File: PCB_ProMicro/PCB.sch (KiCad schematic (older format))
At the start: 98 parts, among them SW1 SW_Push, SW10 SW_Push, SW11 SW_Push, SW12 SW_Push, SW13 SW_Push, SW14 SW_Push, SW15 SW_Push, SW16 SW_Push, SW17 SW_Push, SW18 SW_Push, SW19 SW_Push, SW2 SW_Push, SW20 SW_Push, SW21 SW_Push, SW22 SW_Push, SW23 SW_Push, SW24 SW_Push, SW25 SW_Push, SW26 SW_Push, SW27 SW_Push, SW28 SW_Push, SW29 SW_Push, SW3 SW_Push, SW30 SW_Push, SW31 SW_Push, SW32 SW_Push, SW33 SW_Push, SW34 SW_Push, SW35 SW_Push, SW36 SW_Push, SW37 SW_Push, SW38 SW_Push, SW39 SW_Push, SW4 SW_Push, SW40 SW_Push, SW41 SW_Push, SW42 SW_Push, SW43 SW_Push, SW44 SW_Push, SW45 SW_Push, SW46 SW_Push, SW47 SW_Push, SW48 SW_Push, SW49 SW_Push, SW5 SW_Push, SW6 SW_Push, SW7 SW_Push, SW8 SW_Push, SW9 SW_Push

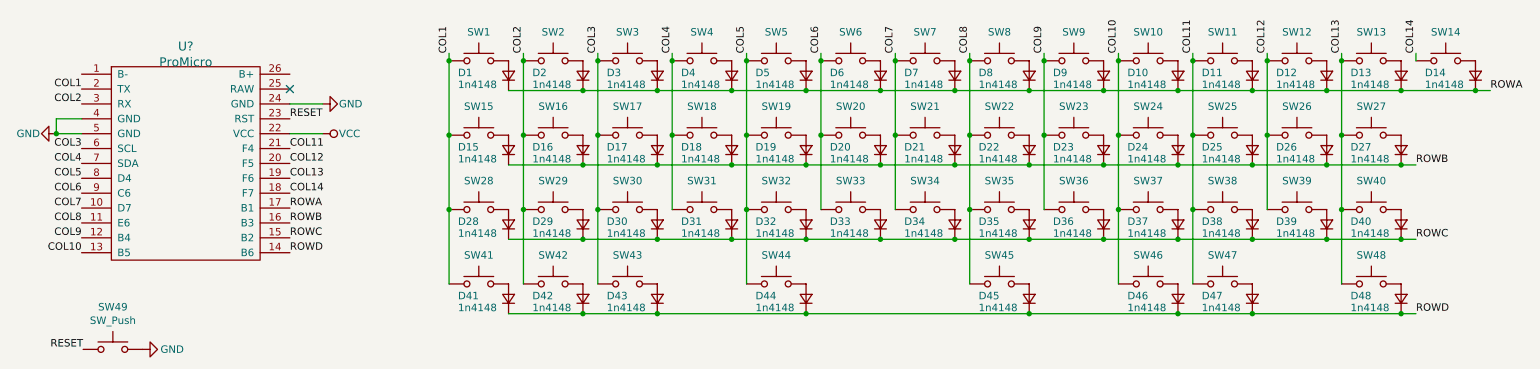
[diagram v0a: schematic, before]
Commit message: Edit pro micro symbol
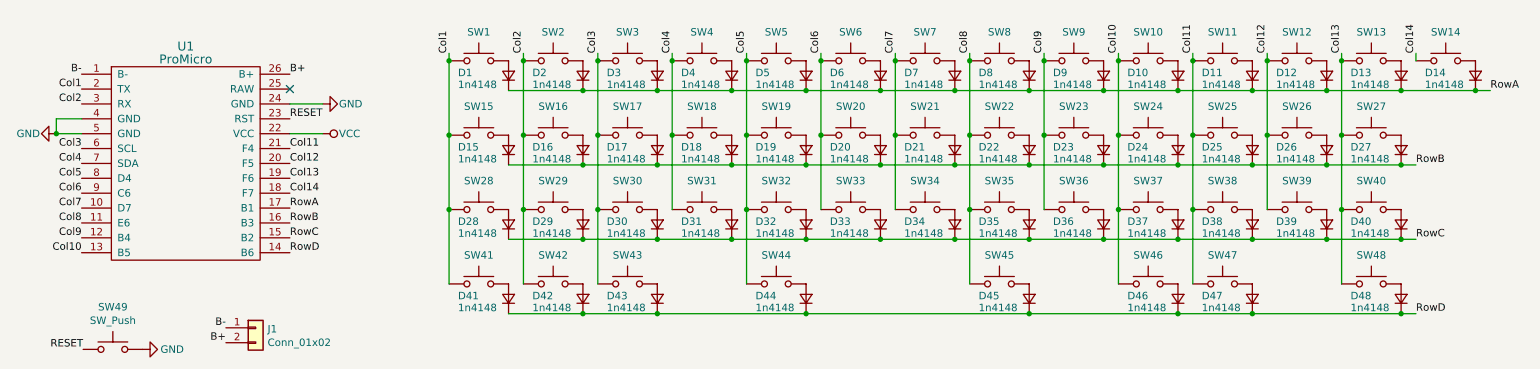
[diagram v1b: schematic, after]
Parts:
- added J1: Conn_01x02, symbol Connector_Generic:Conn_01x02
- gave numbers to parts that had none: 1
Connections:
- net B-: now reaches U1.1 (B-)
- net B-: now also J1.1 (Pin_1)
- net B+: now reaches U1.26 (B+)
- net B+: now also J1.2 (Pin_2)
- net COL1 renamed Col1
- net COL10 renamed Col10
- net COL11 renamed Col11
- net COL12 renamed Col12
- net COL13 renamed Col13
- net COL14 renamed Col14
- net COL2 renamed Col2
- net COL3 renamed Col3
- net COL4 renamed Col4
- net COL5 renamed Col5
- net COL6 renamed Col6
- net COL7 renamed Col7
- net COL8 renamed Col8
- net COL9 renamed Col9
- net ROWA renamed RowA
- net ROWB renamed RowB
- net ROWC renamed RowC
- net ROWD renamed RowD
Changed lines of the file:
@@
 	9800 2380 9300 2380
 Text Label 3900 1130 1    50   ~ 0
-COL1
+Col1
 Text Label 4400 1130 1    50   ~ 0
-COL2
+Col2
 Text Label 4900 1130 1    50   ~ 0
-COL3
+Col3
 Text Label 5400 1130 1    50   ~ 0
-COL4
+Col4
 Text Label 5900 1130 1    50   ~ 0
-COL5
+Col5
 Text Label 6400 1130 1    50   ~ 0
-COL6
+Col6
 Text Label 6900 1130 1    50   ~ 0
-COL7
+Col7
 Text Label 7400 1130 1    50   ~ 0
-COL8
+Col8
 Text Label 7900 1130 1    50   ~ 0
-COL9
+Col9
 Text Label 8400 1130 1    50   ~ 0
-COL10
+Col10
 Text Label 8900 1130 1    50   ~ 0
-COL11
+Col11
 Text Label 9400 1130 1    50   ~ 0
-COL12
+Col12
 Text Label 9900 1130 1    50   ~ 0
-COL13
+Col13
 Text Label 10400 1130 1    50   ~ 0
-COL14
+Col14
 Text Label 10900 1380 0    50   ~ 0
-ROWA
+RowA
 Text Label 10400 1880 0    50   ~ 0
-ROWB
+RowB
 Text Label 10400 2380 0    50   ~ 0
-ROWC
+RowC
 Wire Wire Line
 	10400 2380 10300 2380
@@
 	9300 2880 10300 2880
 Text Label 10400 2880 0    50   ~ 0
-ROWD
+RowD
 Wire Wire Line
 	10400 2880 10300 2880
@@
 $EndComp
 $Comp
-L promicro:ProMicro U?
+L promicro:ProMicro U1
 U 1 1 5ED7E469
 P 2130 2120
-F 0 "U?" H 2130 3157 60  0000 C CNN
-F 1 "ProMicro" H 2130 3051 60  0000 C CNN
+F 0 "U1" H 2130 3157 60  0000 C CNN
+F 1 "ProMicro" H 2130 3070 60  0000 C CNN
 F 2 "" H 2230 1070 60  0000 C CNN
 F 3 "" H 2230 1070 60  0000 C CNN
@@
 $EndComp
 $Comp
-L power:GND #PWR?
+L power:GND #PWR0101
 U 1 1 5ED825B3
 P 3050 1470
-F 0 "#PWR?" H 3050 1220 50  0001 C CNN
+F 0 "#PWR0101" H 3050 1220 50  0001 C CNN
 F 1 "GND" V 3050 1360 50  0000 R CNN
 F 2 "" H 3050 1470 50  0001 C CNN
@@
 $EndComp
 $Comp
-L power:GND #PWR?
+L power:GND #PWR0102
 U 1 1 5ED85438
 P 1260 1670
-F 0 "#PWR?" H 1260 1420 50  0001 C CNN
+F 0 "#PWR0102" H 1260 1420 50  0001 C CNN
 F 1 "GND" V 1260 1560 50  0000 R CNN
 F 2 "" H 1260 1670 50  0001 C CNN
@@
 $EndComp
 $Comp
-L power:VCC #PWR?
+L power:VCC #PWR0103
 U 1 1 5ED8AD67
 P 3050 1670
-F 0 "#PWR?" H 3050 1520 50  0001 C CNN
+F 0 "#PWR0103" H 3050 1520 50  0001 C CNN
 F 1 "VCC" V 3050 1780 50  0000 L CNN
 F 2 "" H 3050 1670 50  0001 C CNN
@@
 NoConn ~ 2830 1370
 Text Label 1430 1370 2    50   ~ 0
-COL1
+Col1
 Text Label 1430 1470 2    50   ~ 0
-COL2
+Col2
 Text Label 1430 1770 2    50   ~ 0
-COL3
+Col3
 Text Label 1430 1870 2    50   ~ 0
-COL4
+Col4
 Text Label 1430 2070 2    50   ~ 0
-COL6
+Col6
 Text Label 1430 1970 2    50   ~ 0
-COL5
+Col5
 Text Label 1430 2170 2    50   ~ 0
-COL7
+Col7
 Text Label 1430 2270 2    50   ~ 0
-COL8
+Col8
 Text Label 1430 2370 2    50   ~ 0
-COL9
+Col9
 Text Label 1430 2470 2    50   ~ 0
-COL10
+Col10
 Wire Wire Line
 	1260 1670 1430 1670
@@
 Connection ~ 1260 1670
 Text Label 2830 1770 0    50   ~ 0
-COL11
+Col11
 Text Label 2830 1870 0    50   ~ 0
-COL12
+Col12
 Text Label 2830 1970 0    50   ~ 0
-COL13
+Col13
 Text Label 2830 2070 0    50   ~ 0
-COL14
+Col14
 Text Label 2830 2170 0    50   ~ 0
-ROWA
+RowA
 Text Label 2830 2270 0    50   ~ 0
-ROWB
+RowB
 Text Label 2830 2370 0    50   ~ 0
-ROWC
+RowC
 Text Label 2830 2470 0    50   ~ 0
-ROWD
+RowD
 Text Label 2830 1570 0    50   ~ 0
 RESET
@@
 Text Label 1440 3120 2    50   ~ 0
 RESET
+$Comp
+L Connector_Generic:Conn_01x02 J1
+U 1 1 5ED706FC
+P 2600 2975
+F 0 "J1" H 2680 2967 50  0000 L CNN
+F 1 "Conn_01x02" H 2680 2876 50  0000 L CNN
+F 2 "" H 2600 2975 50  0001 C CNN
+F 3 "~" H 2600 2975 50  0001 C CNN
+	1    2600 2975
+	1    0    0    -1
+$EndComp
+Text Label 2400 2975 2    50   ~ 0
+B-
+Text Label 2400 3075 2    50   ~ 0
+B+
+Text Label 1430 1270 2    50   ~ 0
+B-
+Text Label 2830 1270 0    50   ~ 0
+B+
 $EndSCHEMATC

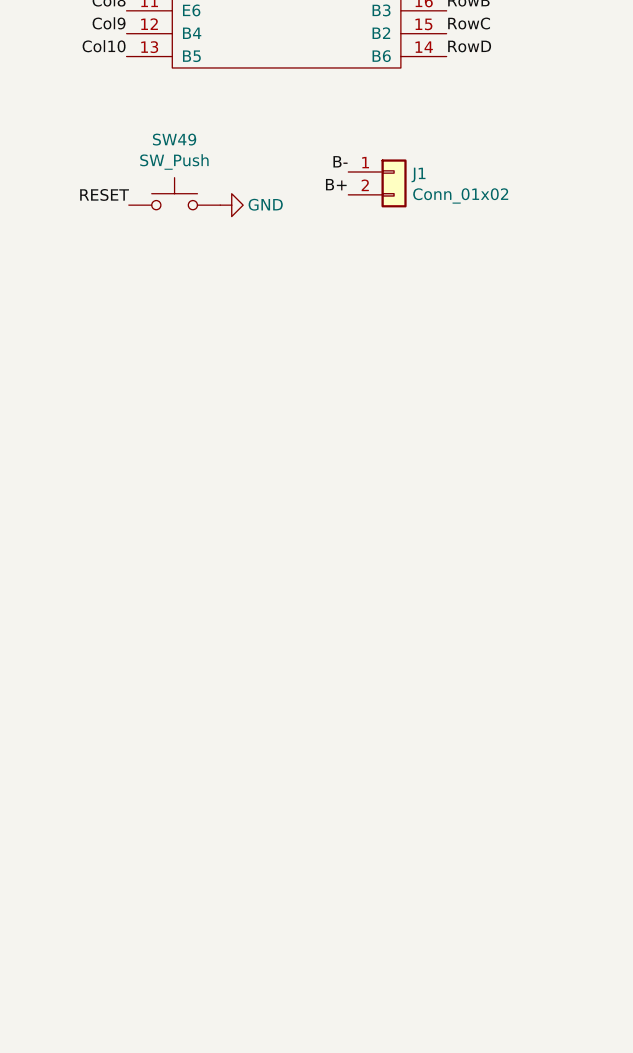
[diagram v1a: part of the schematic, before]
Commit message: Add USB-C into schematic
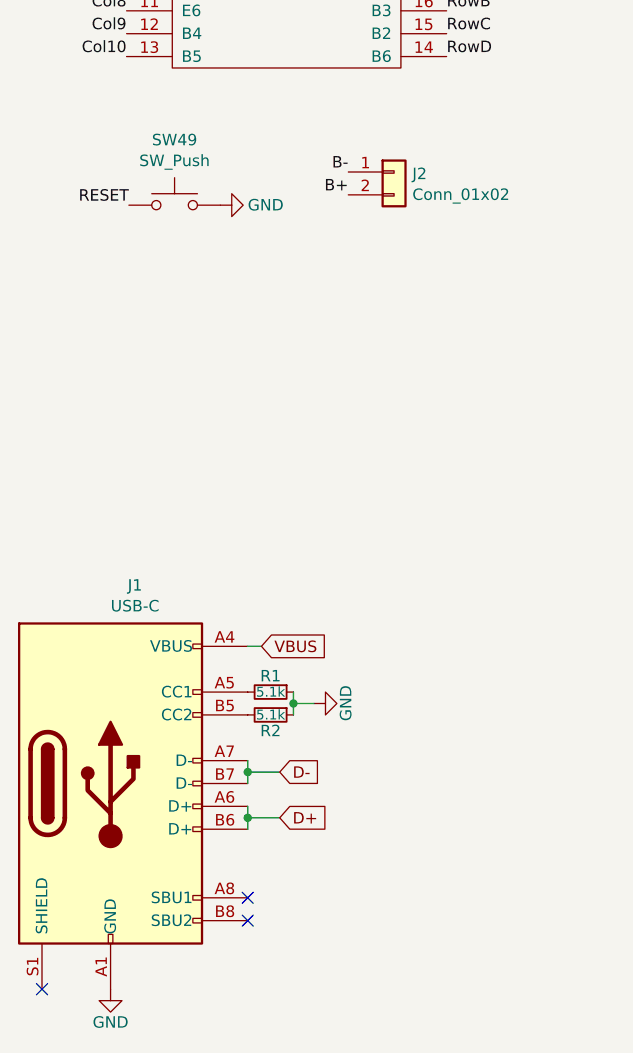
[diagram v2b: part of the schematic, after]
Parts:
- added J1: USB-C, symbol Connector:USB_C_Receptacle_USB2.0
- added R1, R2: 5.1k, symbol Device:R_Small
- renumbered J1 to J2
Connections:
- net GND: now also J1.A1 (GND), J1.A12 (GND), J1.B1 (GND), J1.B12 (GND), R1.1, R2.1
- new net: J1.A5 (CC1), R1.2
- new net: J1.B5 (CC2), R2.2
- new net D+: J1.A6 (D+), J1.B6 (D+)
- new net D-: J1.A7 (D-), J1.B7 (D-)
- new net VBUS: J1.A4 (VBUS), J1.A9 (VBUS), J1.B4 (VBUS), J1.B9 (VBUS)
- no-connect marks 1 -> 4
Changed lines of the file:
@@
 RESET
 $Comp
-L Connector_Generic:Conn_01x02 J1
+L Connector_Generic:Conn_01x02 J2
 U 1 1 5ED706FC
 P 2600 2975
-F 0 "J1" H 2680 2967 50  0000 L CNN
+F 0 "J2" H 2680 2967 50  0000 L CNN
 F 1 "Conn_01x02" H 2680 2876 50  0000 L CNN
 F 2 "" H 2600 2975 50  0001 C CNN
@@
 Text Label 2830 1270 0    50   ~ 0
 B+
+$Comp
+L Connector:USB_C_Receptacle_USB2.0 J1
+U 1 1 5EDB247E
+P 1360 5650
+F 0 "J1" H 1467 6517 50  0000 C CNN
+F 1 "USB-C" H 1467 6426 50  0000 C CNN
+F 2 "" H 1510 5650 50  0001 C CNN
+F 3 "https://www.usb.org/sites/default/files/documents/usb_type-c.zip" H 1510 5650 50  0001 C CNN
+	1    1360 5650
+	1    0    0    -1
+$EndComp
+Text GLabel 2100 5600 2    50   Input ~ 0
+D-
+Wire Wire Line
+	1960 5550 1960 5600
+Wire Wire Line
+	2100 5600 1960 5600
+Connection ~ 1960 5600
+Wire Wire Line
+	1960 5600 1960 5650
+Text GLabel 2100 5800 2    50   Input ~ 0
+D+
+Wire Wire Line
+	1960 5750 1960 5800
+Wire Wire Line
+	2100 5800 1960 5800
+Connection ~ 1960 5800
+Wire Wire Line
+	1960 5800 1960 5850
+$Comp
+L power:GND #PWR?
+U 1 1 5EDC59F6
+P 1360 6550
+F 0 "#PWR?" H 1360 6300 50  0001 C CNN
+F 1 "GND" H 1360 6405 50  0000 C CNN
+F 2 "" H 1360 6550 50  0001 C CNN
+F 3 "" H 1360 6550 50  0001 C CNN
+	1    1360 6550
+	1    0    0    -1
+$EndComp
+$Comp
+L Device:R_Small R1
+U 1 1 5EDC6E57
+P 2060 5250
+F 0 "R1" V 1990 5250 50  0000 C CNN
+F 1 "5.1k" V 2060 5250 43  0000 C CNN
+F 2 "" H 2060 5250 50  0001 C CNN
+F 3 "~" H 2060 5250 50  0001 C CNN
+	1    2060 5250
+	0    1    1    0
+$EndComp
+$Comp
+L Device:R_Small R2
+U 1 1 5EDC82FE
+P 2060 5350
+F 0 "R2" V 2130 5350 50  0000 C CNN
+F 1 "5.1k" V 2060 5350 43  0000 C CNN
+F 2 "" H 2060 5350 50  0001 C CNN
+F 3 "~" H 2060 5350 50  0001 C CNN
+	1    2060 5350
+	0    1    1    0
+$EndComp
+$Comp
+L power:GND #PWR?
+U 1 1 5EDCBE4E
+P 2250 5300
+F 0 "#PWR?" H 2250 5050 50  0001 C CNN
+F 1 "GND" H 2330 5160 50  0000 R CNN
+F 2 "" H 2250 5300 50  0001 C CNN
+F 3 "" H 2250 5300 50  0001 C CNN
+	1    2250 5300
+	0    -1   -1   0
+$EndComp
+Wire Wire Line
+	2160 5250 2160 5300
+Wire Wire Line
+	2250 5300 2160 5300
+Connection ~ 2160 5300
+Wire Wire Line
+	2160 5300 2160 5350
+Text GLabel 2020 5050 2    50   Input ~ 0
+VBUS
+Wire Wire Line
+	2020 5050 1960 5050
+NoConn ~ 1060 6550
+NoConn ~ 1960 6150
+NoConn ~ 1960 6250
 $EndSCHEMATC

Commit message: Add ESD protection diode
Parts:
- added U?: USBLC6-2SC6, Package_TO_SOT_SMD:SOT-23-6, symbol Power_Protection:USBLC6-2SC6
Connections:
- net D+: now also U?.1 (IO1); no longer J1.A6 (D+), J1.B6 (D+)
- net D-: now also U?.3 (IO2); no longer J1.A7 (D-), J1.B7 (D-)
- net GND: now also U?.2 (GND)
- net VBUS: now also U?.5 (VBUS)
- new net USB_D+: J1.A6 (D+), J1.B6 (D+), U?.6 (IO1)
- new net USB_D-: J1.A7 (D-), J1.B7 (D-), U?.4 (IO2)
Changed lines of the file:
@@
 $EndComp
 Text GLabel 2100 5600 2    50   Input ~ 0
-D-
+USB_D-
 Wire Wire Line
 	1960 5550 1960 5600
@@
 	1960 5600 1960 5650
 Text GLabel 2100 5800 2    50   Input ~ 0
-D+
+USB_D+
 Wire Wire Line
 	1960 5750 1960 5800
@@
 NoConn ~ 1960 6150
 NoConn ~ 1960 6250
+$Comp
+L Power_Protection:USBLC6-2SC6 U?
+U 1 1 5EDE97BF
+P 3865 5775
+F 0 "U?" H 3865 6635 50  0000 C CNN
+F 1 "USBLC6-2SC6" H 3865 6560 50  0000 C CNN
+F 2 "Package_TO_SOT_SMD:SOT-23-6" H 3115 6175 50  0001 C CNN
+F 3 "http://www2.st.com/resource/en/datasheet/CD00050750.pdf" H 4065 6125 50  0001 C CNN
+	1    3865 5775
+	1    0    0    -1
+$EndComp
+Text GLabel 3365 5675 0    50   Input ~ 0
+USB_D+
+Text GLabel 4365 5675 2    50   Input ~ 0
+USB_D-
+Text GLabel 3365 5875 0    50   Input ~ 0
+D+
+Text GLabel 4365 5875 2    50   Input ~ 0
+D-
+$Comp
+L power:GND #PWR?
+U 1 1 5EDF1287
+P 3865 6275
+F 0 "#PWR?" H 3865 6025 50  0001 C CNN
+F 1 "GND" H 3865 6135 50  0000 C CNN
+F 2 "" H 3865 6275 50  0001 C CNN
+F 3 "" H 3865 6275 50  0001 C CNN
+	1    3865 6275
+	1    0    0    -1
+$EndComp
+Text GLabel 3865 5275 1    50   Input ~ 0
+VBUS
 $EndSCHEMATC

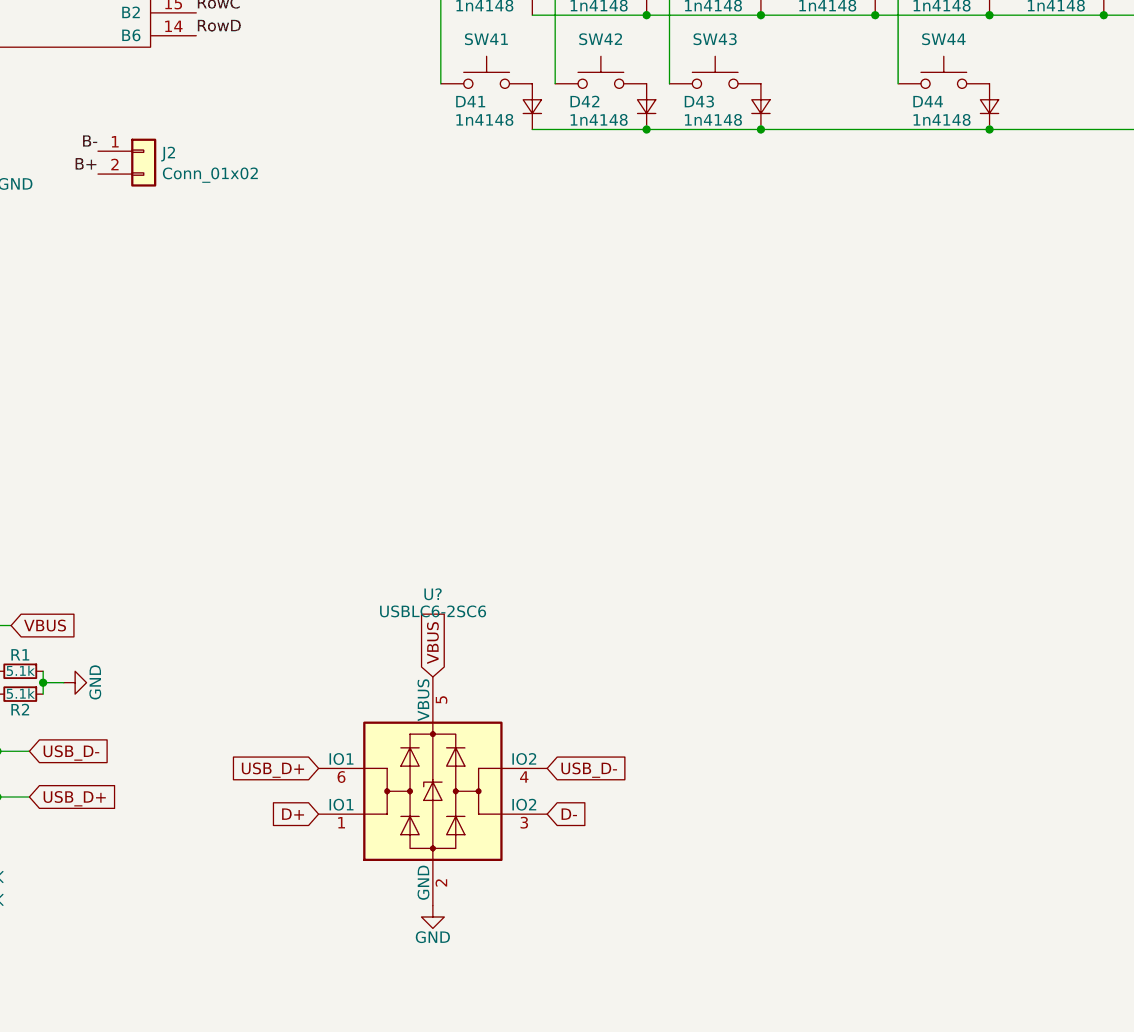
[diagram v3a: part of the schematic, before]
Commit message: Add 4 pit connector for USB
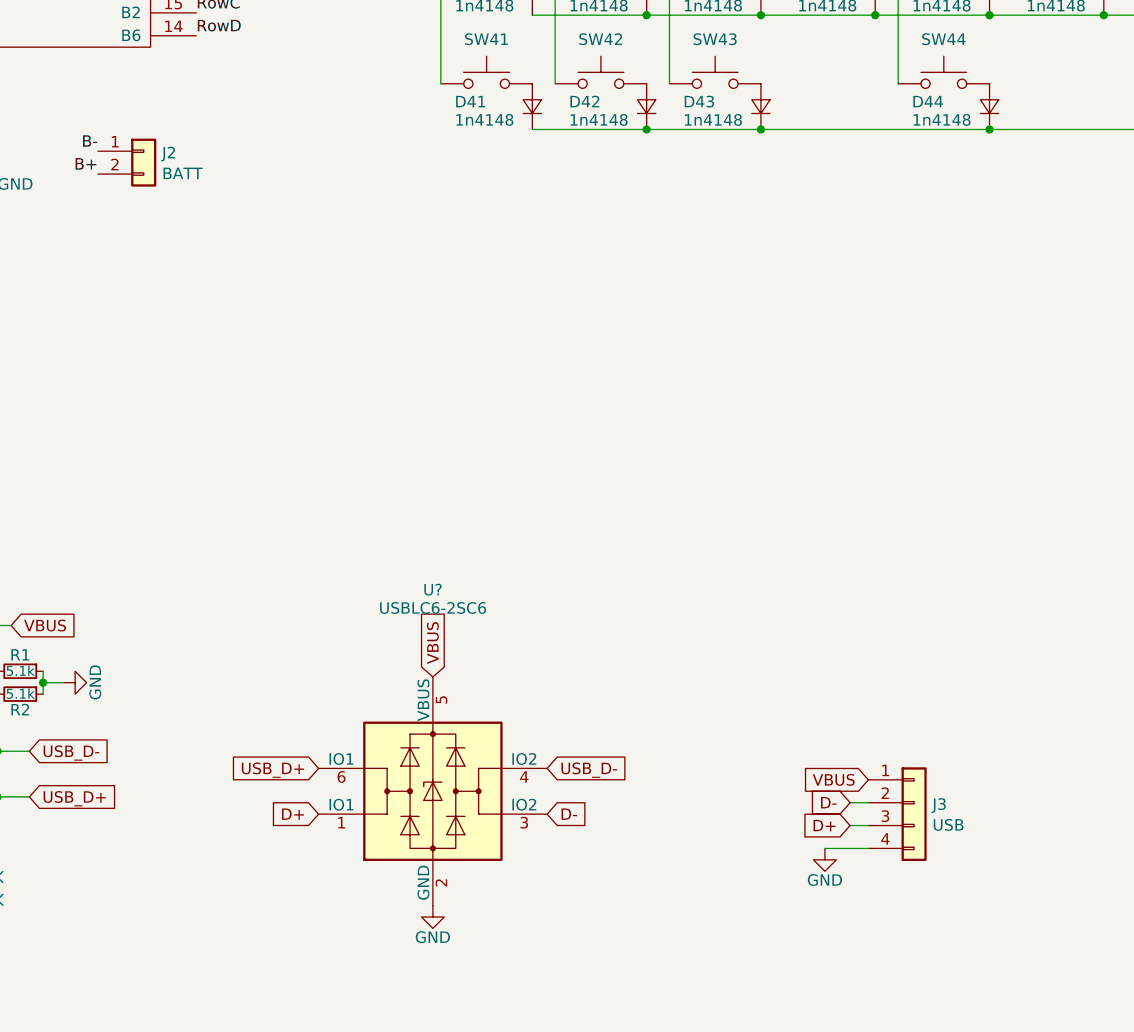
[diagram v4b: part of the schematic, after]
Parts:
- added J3: USB, symbol Connector_Generic:Conn_01x04
- J2: value Conn_01x02 -> BATT
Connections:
- net D+: now also J3.3 (Pin_3)
- net D-: now also J3.2 (Pin_2)
- net GND: now also J3.4 (Pin_4)
- net VBUS: now also J3.1 (Pin_1)
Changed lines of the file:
@@
 P 2600 2975
 F 0 "J2" H 2680 2967 50  0000 L CNN
-F 1 "Conn_01x02" H 2680 2876 50  0000 L CNN
+F 1 "BATT" H 2680 2876 50  0000 L CNN
 F 2 "" H 2600 2975 50  0001 C CNN
 F 3 "~" H 2600 2975 50  0001 C CNN
@@
 U 1 1 5EDE97BF
 P 3865 5775
-F 0 "U?" H 3865 6635 50  0000 C CNN
-F 1 "USBLC6-2SC6" H 3865 6560 50  0000 C CNN
+F 0 "U?" H 3865 6655 50  0000 C CNN
+F 1 "USBLC6-2SC6" H 3865 6575 50  0000 C CNN
 F 2 "Package_TO_SOT_SMD:SOT-23-6" H 3115 6175 50  0001 C CNN
 F 3 "http://www2.st.com/resource/en/datasheet/CD00050750.pdf" H 4065 6125 50  0001 C CNN
@@
 Text GLabel 3865 5275 1    50   Input ~ 0
 VBUS
+$Comp
+L Connector_Generic:Conn_01x04 J3
+U 1 1 5EDF46E2
+P 5970 5825
+F 0 "J3" H 6050 5817 50  0000 L CNN
+F 1 "USB" H 6050 5726 50  0000 L CNN
+F 2 "" H 5970 5825 50  0001 C CNN
+F 3 "~" H 5970 5825 50  0001 C CNN
+	1    5970 5825
+	1    0    0    -1
+$EndComp
+Text GLabel 5770 5725 0    50   Input ~ 0
+VBUS
+Text GLabel 5690 5825 0    50   Input ~ 0
+D-
+Text GLabel 5690 5925 0    50   Input ~ 0
+D+
+Wire Wire Line
+	5690 5925 5770 5925
+Wire Wire Line
+	5690 5825 5770 5825
+$Comp
+L power:GND #PWR?
+U 1 1 5EE00720
+P 5580 6025
+F 0 "#PWR?" H 5580 5775 50  0001 C CNN
+F 1 "GND" H 5580 5885 50  0000 C CNN
+F 2 "" H 5580 6025 50  0001 C CNN
+F 3 "" H 5580 6025 50  0001 C CNN
+	1    5580 6025
+	1    0    0    -1
+$EndComp
+Wire Wire Line
+	5580 6025 5770 6025
 $EndSCHEMATC
